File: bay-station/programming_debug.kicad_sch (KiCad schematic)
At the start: 2 parts, among them J3 Conn_ARM_JTAG_SWD_10, SW2 RESET

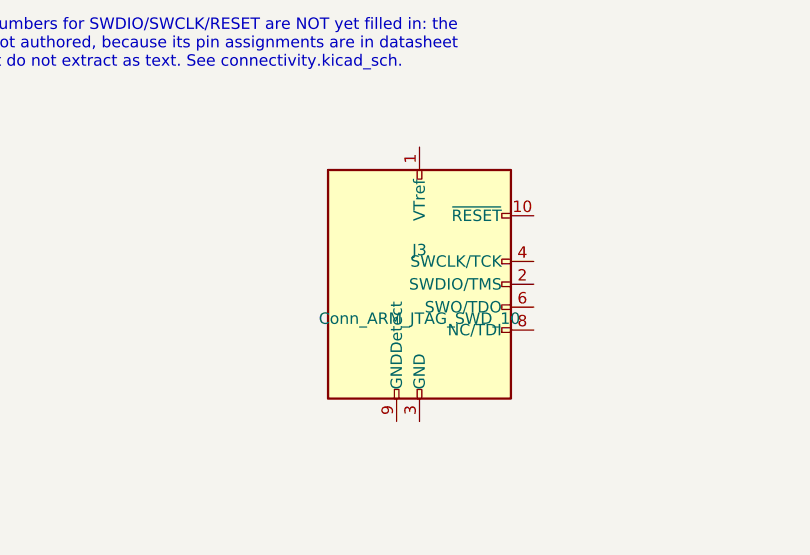
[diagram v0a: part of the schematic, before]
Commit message: Wire up power_bms, regulation and programming_debug; tie off floating grounds
The bay station was built entirely from global labels and power symbols --
zero drawn wires on any sheet. This starts converting the power path to
explicit wiring and connects the grounds that were left floating:

- power_bms: 62 wires; 31 label justifications flipped left->right where
  the labels were mirrored. No symbols added or removed.
- regulation: 11 wires, 3 junctions, 5 GND symbols (#PWR01-05).
- programming_debug: 2 wires, 1 junction, 1 GND symbol (#PWR06).

ERC goes 518 -> 497 violations (494 -> 473 errors), entirely in
pin_not_connected (360 -> 342), power_pin_not_driven (98 -> 96) and
pin_not_driven (36 -> 35). Nothing regressed. The remaining 342
pin_not_connected are the sheets that are still label-only.

Unavoidable churn in this commit: KiCad 10 re-serialized seven sheets from
8.0 format (version 20231120) to 10.0 (20260306) on save -- clock_dist,
connectivity, gnss, indicators, programming_debug, testpoints, uwb_array.
That accounts for most of the diff; those seven have no content change
beyond it. CLAUDE.md asks that the format not be bumped as a side effect,
but it cannot be split out here: kicad-cli sch upgrade serializes
differently from the GUI and leaves ~3700 lines of residual churn, so a
format-only commit would be tidier in shape and no more honest. Four
sheets were already on 10.0 format before this commit.

Co-Authored-By: Claude Opus 5 (1M context) <noreply@anthropic.com>
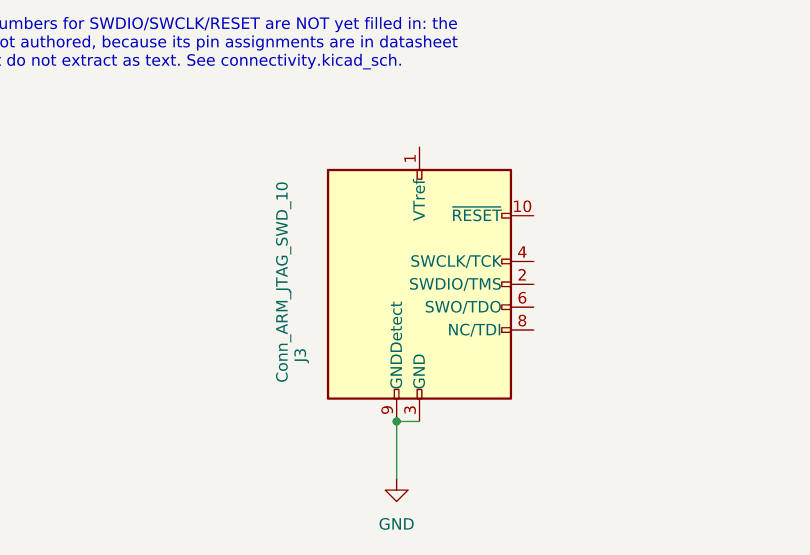
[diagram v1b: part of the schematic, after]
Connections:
- net GND: now reaches J3.3 (GND), J3.5 (GND)
- net GND: now also J3.9 (GNDDetect)
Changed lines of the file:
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@@
 (kicad_sch
-	(version 20231120)
+	(version 20260306)
 	(generator "eeschema")
-	(generator_version "8.0")
+	(generator_version "10.0")
 	(paper "A4")
 	(title_block
@@
 	)
 	(text "Programming / Debug -- SWD"
-		(at 30.48 25.40 0)
+		(exclude_from_sim no)
+		(at 30.48 25.4 0)
 		(effects
 			(font
@@
 	)
 	(text "This sheet collapsed when the host moved from ESP32-S3 to the Nordic\nBT840. Nordic parts program over SWD, so nearly all of the previous\ncontents were ESP32-specific and have been deleted:\n\n- R18-R21, the GPIO0/GPIO3/GPIO45/GPIO46 boot-strapping pulls. Nordic has\n  no equivalent boot-strap pins.\n- R22 + C23, the EN reset RC delay. The nRF52840 has an internal power-on\n  reset; no external RC is needed.\n- SW1, the BOOT button. There is no boot-mode pin to hold.\n- J3 + R23/R24, the data-capable USB-C and its CC pull-downs, which existed\n  ONLY so the ESP32-S3 could be flashed over native USB.\n\nThat last deletion RESOLVES the long-standing 'two USB-C connectors' open\nitem, by removal rather than by choosing between them. The board is back to\none USB-C, the power-only J2 on power_bms.kicad_sch.\n\nWhat remains is what a Nordic part actually needs: an SWD header and a\nreset button.\n\nJ3 (reference reused, the old one is gone) is the same 2x5 1.27mm ARM\nCortex Debug connector already used on the wristband -- deliberately the\nsame part on both boards so one debug probe and one cable serve the whole\nproject. SWDIO and SWCLK go to the BT840; VTref to +3V3_SYS so the probe's\nlevel shifters reference the right rail; nRESET to the BT840's reset pin,\nthe same node SW2 pulls down.\n\nSW2 keeps its reference from the previous revision. Its function is\nunchanged -- it was the RESET button then and it is the RESET button now."
+		(exclude_from_sim no)
 		(at 30.48 33.02 0)
 		(effects
@@
 	)
 	(text "Exact BT840 pin numbers for SWDIO/SWCLK/RESET are NOT yet filled in: the\nBT840 symbol is not authored, because its pin assignments are in datasheet\nfigures that do not extract as text. See connectivity.kicad_sch."
+		(exclude_from_sim no)
 		(at 30.48 118.11 0)
 		(effects
@@
 		)
 	)
+	(junction
+		(at 57.15 160.02)
+		(diameter 0)
+		(color 0 0 0 0)
+	)
+	(wire
+		(pts
+			(xy 57.15 166.37) (xy 57.15 160.02)
+		)
+		(stroke
+			(width 0)
+			(type default)
+		)
+	)
+	(wire
+		(pts
+			(xy 57.15 160.02) (xy 59.69 160.02)
+		)
+		(stroke
+			(width 0)
+			(type default)
+		)
+	)
 	(symbol
 		(lib_id "Connector:Conn_ARM_JTAG_SWD_10")
 		(at 59.69 144.78 0)
 		(unit 1)
+		(body_style 1)
 		(exclude_from_sim no)
 		(in_bom yes)
 		(on_board yes)
+		(in_pos_files yes)
 		(dnp no)
 		(property "Reference" "J3"
-			(at 59.69 140.97 0)
+			(at 46.482 152.654 90)
+			(show_name no)
+			(do_not_autoplace no)
 			(effects
 				(font
@@
 		)
 		(property "Value" "Conn_ARM_JTAG_SWD_10"
-			(at 59.69 148.59 0)
+			(at 44.45 144.526 90)
+			(show_name no)
+			(do_not_autoplace no)
 			(effects
 				(font
@@
 		(property "Footprint" "Connector_PinHeader_1.27mm:PinHeader_2x05_P1.27mm_Vertical"
 			(at 59.69 144.78 0)
-			(effects
-				(font
-					(size 1.27 1.27)
-				)
-				(hide yes)
-			)
-		)
-		(property "Datasheet" "~"
+			(hide yes)
+			(show_name no)
+			(do_not_autoplace no)
+			(effects
+				(font
+					(size 1.27 1.27)
+				)
+			)
+		)
+		(property "Datasheet" ""
 			(at 59.69 144.78 0)
-			(effects
-				(font
-					(size 1.27 1.27)
-				)
-				(hide yes)
+			(hide yes)
+			(show_name no)
+			(do_not_autoplace no)
+			(effects
+				(font
+					(size 1.27 1.27)
+				)
 			)
 		)
 		(property "Description" "ARM Cortex Debug SWD header for the BT840 (nRF52840). Same part as the wristband's J3 so one probe and cable serve both boards."
 			(at 59.69 144.78 0)
-			(effects
-				(font
-					(size 1.27 1.27)
-				)
-				(hide yes)
-			)
+			(hide yes)
+			(show_name no)
+			(do_not_autoplace no)
+			(effects
+				(font
+					(size 1.27 1.27)
+				)
+			)
+		)
+		(pin "1"
+		)
+		(pin "2"
+		)
+		(pin "3"
+		)
+		(pin "4"
+		)
+		(pin "5"
+		)
+		(pin "6"
+		)
+		(pin "7"
+		)
+		(pin "8"
+		)
+		(pin "9"
+		)
+		(pin "10"
 		)
 		(instances
@@
 		(at 119.38 144.78 0)
 		(unit 1)
+		(body_style 1)
 		(exclude_from_sim no)
 		(in_bom yes)
 		(on_board yes)
+		(in_pos_files yes)
 		(dnp no)
 		(property "Reference" "SW2"
 			(at 119.38 140.97 0)
+			(show_name no)
+			(do_not_autoplace no)
 			(effects
 				(font
@@
 		(property "Value" "RESET"
 			(at 119.38 148.59 0)
+			(show_name no)
+			(do_not_autoplace no)
 			(effects
 				(font
@@
 		(property "Footprint" ""
 			(at 119.38 144.78 0)
-			(effects
-				(font
-					(size 1.27 1.27)
-				)
-				(hide yes)
-			)
-		)
-		(property "Datasheet" "~"
+			(hide yes)
+			(show_name no)
+			(do_not_autoplace no)
+			(effects
+				(font
+					(size 1.27 1.27)
+				)
+			)
+		)
+		(property "Datasheet" ""
 			(at 119.38 144.78 0)
-			(effects
-				(font
-					(size 1.27 1.27)
-				)
-				(hide yes)
+			(hide yes)
+			(show_name no)
+			(do_not_autoplace no)
+			(effects
+				(font
+					(size 1.27 1.27)
+				)
 			)
 		)
 		(property "Description" "Reset button, pulling the BT840's active-low reset to ground. Footprint to be chosen at BOM time, same as the previous revision."
 			(at 119.38 144.78 0)
-			(effects
-				(font
-					(size 1.27 1.27)
-				)
-				(hide yes)
-			)
+			(hide yes)
+			(show_name no)
+			(do_not_autoplace no)
+			(effects
+				(font
+					(size 1.27 1.27)
+				)
+			)
+		)
+		(pin "1"
+		)
+		(pin "2"
 		)
 		(instances
@@
 					(unit 1)
 				)
+			)
+		)
+	)
+	(symbol
+		(lib_id "power:GND")
+		(at 57.15 166.37 0)
+		(unit 1)
+		(body_style 1)
+		(exclude_from_sim no)
+		(in_bom yes)
+		(on_board yes)
+		(in_pos_files yes)
+		(dnp no)
+		(fields_autoplaced yes)
+		(property "Reference" "#PWR06"
+			(at 57.15 172.72 0)
+			(hide yes)
+			(show_name no)
+			(do_not_autoplace no)
+			(effects
+				(font
+					(size 1.27 1.27)
+				)
+			)
+		)
+		(property "Value" "GND"
+			(at 57.15 171.45 0)
+			(show_name no)
+			(do_not_autoplace no)
+			(effects
+				(font
+					(size 1.27 1.27)
+				)
+			)
+		)
+		(property "Footprint" ""
+			(at 57.15 166.37 0)
+			(hide yes)
+			(show_name no)
+			(do_not_autoplace no)
+			(effects
+				(font
+					(size 1.27 1.27)
+				)
+			)
+		)
+		(property "Datasheet" ""
+			(at 57.15 166.37 0)
+			(hide yes)
+			(show_name no)
+			(do_not_autoplace no)
+			(effects
+				(font
+					(size 1.27 1.27)
+				)
+			)
+		)
+		(property "Description" "Power symbol creates a global label with name \"GND\" , ground"
+			(at 57.15 166.37 0)
+			(hide yes)
+			(show_name no)
+			(do_not_autoplace no)
+			(effects
+				(font
+					(size 1.27 1.27)
+				)
+			)
+		)
+		(pin "1"
+		)
+		(instances
+			(project "bay-station"
+				(path "/543ba435-6cf4-448c-821e-3c5778b02e9c/883ff08c-ad9f-4863-b9db-49772b53748e"
+					(reference "#PWR06")
+					(unit 1)
+				)
